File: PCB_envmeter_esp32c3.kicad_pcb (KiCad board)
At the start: 2 copper layers, 72 x 47.5 mm, 31 parts, among them J1 USB_C_Receptacle_USB2.0_16P, J3 AE-BME680, J4 SSD1306, Q1 2SC2001, SW1 Reset, SW2 Mode, U1 ESP32-C3-WROOM-02, U2 AP7333-33SAG, U3 NJM2845DL1-33

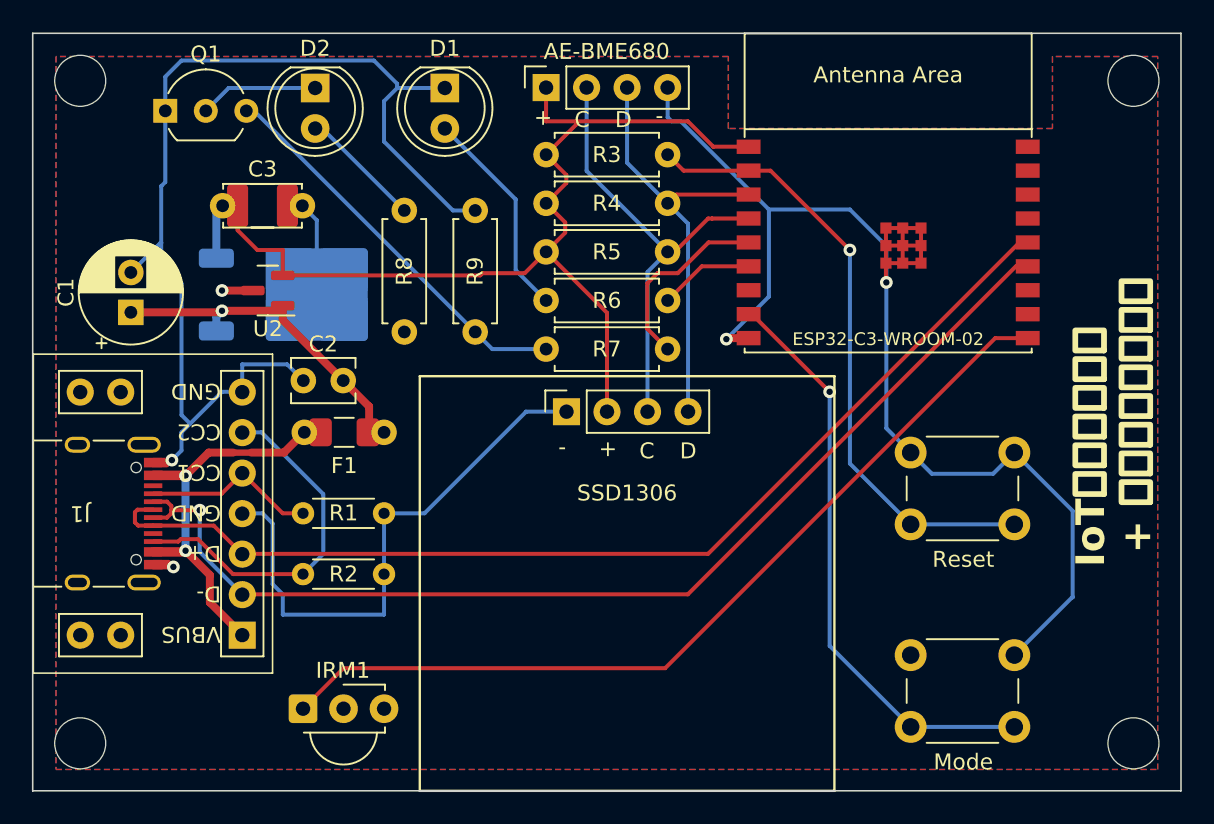
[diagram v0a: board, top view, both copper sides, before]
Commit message: Replace OSRB38C9AA symbol
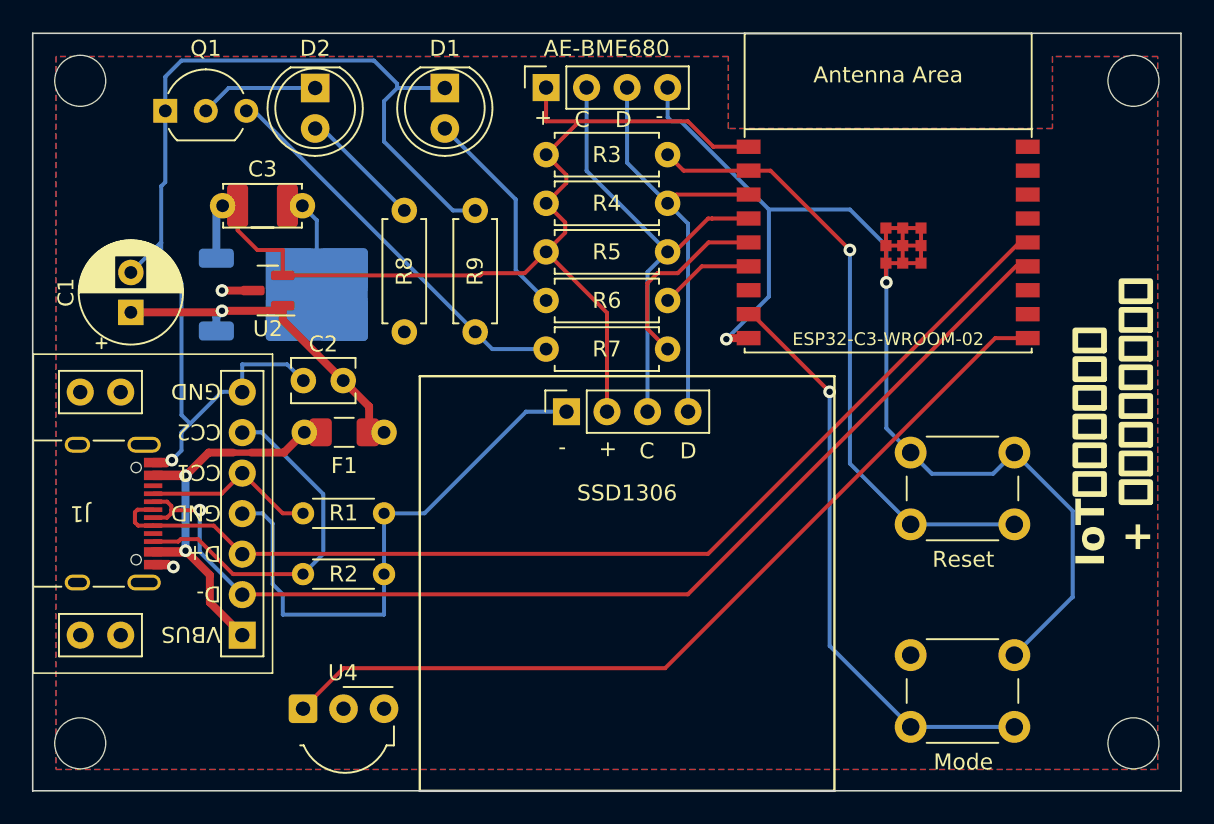
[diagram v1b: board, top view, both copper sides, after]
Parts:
- removed IRM1: OSRB38C9AA, OptoDevice:Vishay_MINICAST-3Pin
- added U4: OSRB38C9AA, OptoDevice:Vishay_MOLD-3Pin, F.Cu at (52.1, 77.0)
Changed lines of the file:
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@@
   (title_block
     (title "IoT環境メーター / スマートリモコン")
-    (date "2024-03-01")
+    (date "2024-03-02")
     (rev "2")
     (company "K.Takata")
@@
     )
   )
-  (footprint "OptoDevice:Vishay_MINICAST-3Pin" (layer "F.Cu")
-    (at 52.07 77.02)
-    (descr "IR Receiver Vishay TSOP-xxxx, MINICAST package, see https://www.vishay.com/docs/82669/tsop32s40f.pdf")
-    (tags "IR Receiver Vishay TSOP-xxxx MINICAST")
-    (property "Sheetfile" "PCB_envmeter_esp32c3.kicad_sch")
-    (property "Sheetname" "")
-    (property "ki_description" "Infrared Receiver Module")
-    (attr through_hole)
-    (fp_text reference "IRM1" (at 2.5 -2.4 180) (layer "F.SilkS")
-        (effects (font (size 1 1) (thickness 0.15)))
-    )
-    (fp_text value "OSRB38C9AA" (at 2.55 4.6 180) (layer "F.Fab")
-        (effects (font (size 1 1) (thickness 0.15)))
-    )
-    (fp_text user "${REFERENCE}" (at 2.54 0) (layer "F.Fab")
-        (effects (font (size 1 1) (thickness 0.15)))
-    )
-    (fp_line (start 5.14 -1.51) (end 2.54 -1.51)
-      (stroke (width 0.12) (type solid)) (layer "F.SilkS"))
-    (fp_line (start 5.14 -1.16) (end 5.14 -1.51)
-      (stroke (width 0.12) (type solid)) (layer "F.SilkS"))
-    (fp_line (start 5.14 1.16) (end 5.14 1.5)
-      (stroke (width 0.12) (type solid)) (layer "F.SilkS"))
-    (fp_line (start 5.14 1.5) (end 0.05 1.5)
-      (stroke (width 0.12) (type solid)) (layer "F.SilkS"))
-    (fp_arc (start 4.64 1.5) (mid 2.540869 3.502379) (end 0.440083 1.501736)
-      (stroke (width 0.12) (type solid)) (layer "F.SilkS"))
-    (fp_line (start -1.15 -1.65) (end -1.15 3.7)
-      (stroke (width 0.05) (type solid)) (layer "F.CrtYd"))
-    (fp_line (start -1.15 -1.65) (end 6.23 -1.65)
-      (stroke (width 0.05) (type solid)) (layer "F.CrtYd"))
-    (fp_line (start 6.23 3.7) (end -1.15 3.7)
-      (stroke (width 0.05) (type solid)) (layer "F.CrtYd"))
-    (fp_line (start 6.23 3.7) (end 6.23 -1.65)
-      (stroke (width 0.05) (type solid)) (layer "F.CrtYd"))
-    (fp_line (start 0.04 1.4) (end 0.04 -0.65)
-      (stroke (width 0.1) (type solid)) (layer "F.Fab"))
-    (fp_line (start 0.79 -1.4) (end 0.04 -0.65)
-      (stroke (width 0.1) (type solid)) (layer "F.Fab"))
-    (fp_line (start 0.79 -1.4) (end 5.04 -1.4)
-      (stroke (width 0.1) (type solid)) (layer "F.Fab"))
-    (fp_line (start 5.04 -1.4) (end 5.04 1.4)
-      (stroke (width 0.1) (type solid)) (layer "F.Fab"))
-    (fp_line (start 5.04 1.4) (end 0.04 1.4)
-      (stroke (width 0.1) (type solid)) (layer "F.Fab"))
-    (fp_arc (start 4.54 1.4) (mid 2.54 3.4) (end 0.54 1.4)
-      (stroke (width 0.1) (type solid)) (layer "F.Fab"))
-    (pad "1" thru_hole roundrect (at 0 0) (size 1.8 1.8) (drill 0.9) (layers "*.Cu" "*.Mask") (roundrect_rratio 0.139)
-      (net 29 "IRin") (pinfunction "OUT") (pintype "output"))
-    (pad "2" thru_hole circle (at 2.54 0) (size 1.8 1.8) (drill 0.9) (layers "*.Cu" "*.Mask")
-      (net 2 "GND") (pinfunction "GND") (pintype "input"))
-    (pad "3" thru_hole circle (at 5.08 0) (size 1.8 1.8) (drill 0.9) (layers "*.Cu" "*.Mask")
-      (net 3 "+3.3V") (pinfunction "VCC") (pintype "input"))
-    (model "${KICAD6_3DMODEL_DIR}/OptoDevice.3dshapes/Vishay_MINICAST-3Pin.wrl"
-      (offset (xyz 0 0 0))
-      (scale (xyz 1 1 1))
-      (rotate (xyz 0 0 0))
-    )
-  )
   (footprint "mylib:Connector_USB_C_simple_combo" (layer "F.Cu")
     (at 48.26 72.408 180)
@@
         (effects (font (size 1 1) (thickness 0.15)))
     )
-    (fp_text value "AE-BME680" (at 2.261 3.8 180) (layer "F.SilkS")
+    (fp_text value "AE-BME680" (at 2.457 3.8 180) (layer "F.SilkS")
         (effects (font (size 1 1) (thickness 0.15)))
     )
@@
     )
   )
+  (footprint "OptoDevice:Vishay_MOLD-3Pin" (layer "F.Cu")
+    (at 52.07 77.02)
+    (descr "IR Receiver Vishay TSOP-xxxx, MOLD package, see https://www.vishay.com/docs/82669/tsop32s40f.pdf")
+    (tags "IR Receiver Vishay TSOP-xxxx MOLD")
+    (property "Sheetfile" "PCB_envmeter_esp32c3.kicad_sch")
+    (property "Sheetname" "")
+    (property "ki_description" "IR Receiver Modules for Remote Control Systems")
+    (property "ki_keywords" "opto IR receiver")
+    (attr through_hole)
+    (fp_text reference "U4" (at 2.5 -2.25 180) (layer "F.SilkS")
+        (effects (font (size 1 1) (thickness 0.15)))
+    )
+    (fp_text value "OSRB38C9AA" (at 2.5 5 180) (layer "F.Fab")
+        (effects (font (size 1 1) (thickness 0.15)))
+    )
+    (fp_text user "${REFERENCE}" (at 2.675 1.316) (layer "F.Fab")
+        (effects (font (size 1 1) (thickness 0.15)))
+    )
+    (fp_line (start 0.04 2.3) (end -0.18 2.3)
+      (stroke (width 0.12) (type solid)) (layer "F.SilkS"))
+    (fp_line (start 5.62 -1.36) (end 2.54 -1.36)
+      (stroke (width 0.12) (type solid)) (layer "F.SilkS"))
+    (fp_line (start 5.7 2.3) (end 5.24 2.3)
+      (stroke (width 0.12) (type solid)) (layer "F.SilkS"))
+    (fp_line (start 5.7 2.3) (end 5.7 1.1)
+      (stroke (width 0.12) (type solid)) (layer "F.SilkS"))
+    (fp_arc (start 5.24 2.3) (mid 2.64 4.023119) (end 0.04 2.3)
+      (stroke (width 0.12) (type solid)) (layer "F.SilkS"))
+    (fp_line (start -1.15 -1.5) (end -1.15 4.13)
+      (stroke (width 0.05) (type solid)) (layer "F.CrtYd"))
+    (fp_line (start -1.15 -1.5) (end 6.23 -1.5)
+      (stroke (width 0.05) (type solid)) (layer "F.CrtYd"))
+    (fp_line (start 6.23 4.13) (end -1.15 4.13)
+      (stroke (width 0.05) (type solid)) (layer "F.CrtYd"))
+    (fp_line (start 6.23 4.13) (end 6.23 -1.5)
+      (stroke (width 0.05) (type solid)) (layer "F.CrtYd"))
+    (fp_line (start -0.2 2.2) (end -0.2 -0.5)
+      (stroke (width 0.1) (type solid)) (layer "F.Fab"))
+    (fp_line (start 0.55 -1.25) (end -0.2 -0.5)
+      (stroke (width 0.1) (type solid)) (layer "F.Fab"))
+    (fp_line (start 0.55 -1.25) (end 5.6 -1.25)
+      (stroke (width 0.1) (type solid)) (layer "F.Fab"))
+    (fp_line (start 5.6 -1.25) (end 5.6 2.2)
+      (stroke (width 0.1) (type solid)) (layer "F.Fab"))
+    (fp_line (start 5.6 2.2) (end -0.2 2.2)
+      (stroke (width 0.1) (type solid)) (layer "F.Fab"))
+    (fp_arc (start 5.14 2.25) (mid 2.651941 3.881274) (end 0.149714 2.271818)
+      (stroke (width 0.1) (type solid)) (layer "F.Fab"))
+    (pad "1" thru_hole roundrect (at 0 0) (size 1.8 1.8) (drill 0.9) (layers "*.Cu" "*.Mask") (roundrect_rratio 0.138)
+      (net 29 "IRin") (pinfunction "OUT") (pintype "output"))
+    (pad "2" thru_hole circle (at 2.54 0) (size 1.8 1.8) (drill 0.9) (layers "*.Cu" "*.Mask")
+      (net 2 "GND") (pinfunction "GND") (pintype "power_in"))
+    (pad "3" thru_hole circle (at 5.08 0) (size 1.8 1.8) (drill 0.9) (layers "*.Cu" "*.Mask")
+      (net 3 "+3.3V") (pinfunction "Vs") (pintype "power_in"))
+    (model "${KICAD6_3DMODEL_DIR}/OptoDevice.3dshapes/Vishay_MOLD-3Pin.wrl"
+      (offset (xyz 0 0 0))
+      (scale (xyz 1 1 1))
+      (rotate (xyz 0 0 0))
+    )
+  )
   (footprint "Connector_PinSocket_2.54mm:PinSocket_1x04_P2.54mm_Vertical" (layer "F.Cu")
     (at 68.59 58.395 90)
@@
     (property "ki_keywords" "Low Noise Audio NPN Transistor")
     (attr through_hole)
-    (fp_text reference "Q1" (at 2.54 -3.56) (layer "F.SilkS")
-        (effects (font (size 1 1) (thickness 0.15)))
-    )
+    (fp_text reference "Q1" (at 2.54 -3.916) (layer "F.SilkS")
+        (effects (font (size 1 1) (thickness 0.15)))
+    )

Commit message: Renumber
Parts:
- renumbered R9 to R8, R8 to R9
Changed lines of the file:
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@@
     (property "Sheetfile" "PCB_envmeter_esp32c3.kicad_sch")
     (property "Sheetname" "")
+    (property "Sim.Enable" "0")
     (property "ki_description" "Resettable fuse, polymeric positive temperature coefficient")
     (property "ki_keywords" "resettable fuse PTC PPTC polyfuse polyswitch")
@@
     (property "ki_keywords" "R res resistor")
     (attr through_hole)
-    (fp_text reference "R9" (at 3.81 0 90) (layer "F.SilkS")
+    (fp_text reference "R8" (at 3.81 0 90) (layer "F.SilkS")
         (effects (font (size 1 1) (thickness 0.15)))
     )
@@
     (property "ki_keywords" "R res resistor")
     (attr through_hole)
-    (fp_text reference "R8" (at 3.81 0 90) (layer "F.SilkS")
+    (fp_text reference "R9" (at 3.81 0 90) (layer "F.SilkS")
         (effects (font (size 1 1) (thickness 0.15)))
     )
@@
     (property "Sheetfile" "PCB_envmeter_esp32c3.kicad_sch")
     (property "Sheetname" "")
+    (property "Sim.Enable" "0")
     (property "ki_description" "Unpolarized capacitor")
     (property "ki_keywords" "cap capacitor")
